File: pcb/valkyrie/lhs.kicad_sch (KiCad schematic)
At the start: 1 part, among them U5 NourK_Core

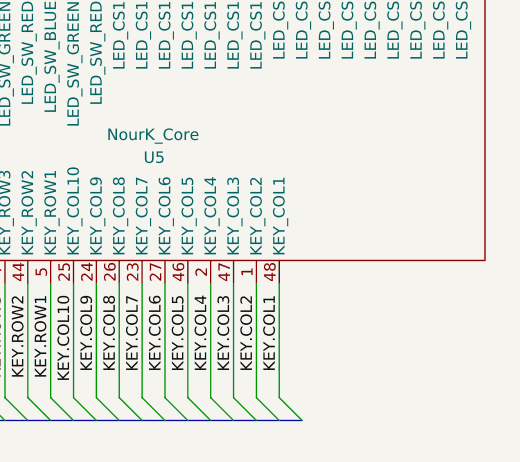
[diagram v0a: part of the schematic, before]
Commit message: Rename project
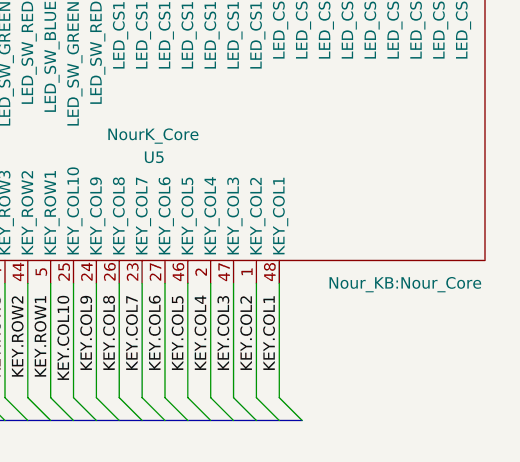
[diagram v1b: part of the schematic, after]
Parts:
- U5: footprint Nour_KB:NourKB_Core_2 -> Nour_KB:Nour_Core; symbol Nour_KB:NourK_Core_3 -> Nour_KB:Nour_Core
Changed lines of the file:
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@@
     (effects (font (size 1.27 1.27)) (justify left bottom))
   )
-  (symbol (lib_id "Nour_KB:NourK_Core_3") (at 172.72 104.14 0) (unit 1)
+  (symbol (lib_id "Nour_KB:Nour_Core") (at 172.72 104.14 0) (unit 1)
     (in_bom no) (on_board yes)
     (property "Reference" "U5" (id 0) (at 173.99 107.95 0)
@@
       (effects (font (size 1.27 1.27)) (justify right))
     )
-    (property "Footprint" "Nour_KB:NourKB_Core_2" (id 2) (at 200.66 121.92 0)
-      (effects (font (size 1.27 1.27)) hide)
-    )
+    (property "Footprint" "Nour_KB:Nour_Core" (id 2) (at 200.66 121.92 0))
     (property "Datasheet" "" (id 3) (at 243.84 100.965 0)
       (effects (font (size 1.27 1.27)) hide)
